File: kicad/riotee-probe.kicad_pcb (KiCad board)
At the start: 2 copper layers, 43.2 x 22.9 mm, 72 parts, among them J1 12402012E212A, J2 Conn_02x05_Odd_Even, J3 Conn_01x05, J4 Conn_01x05, U1 RP2040, U2 W25Q16JVUXIQ, U3 74LVC2T45GT, U4 74LVC2T45GT, U5 74LVC2T45GT, U6 74LVC2T45GT, U7 TLV73325PDBV, U8 TLV73333PDBV, Y1 Crystal_GND24

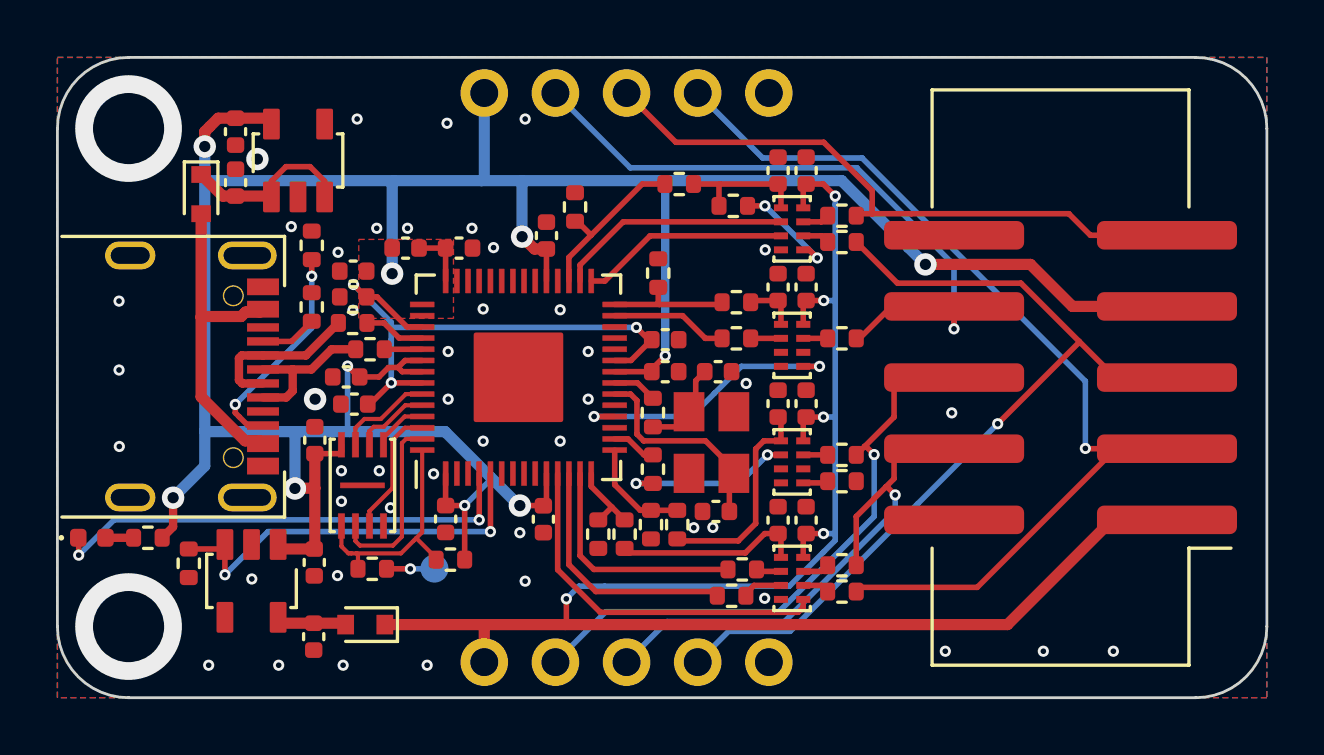
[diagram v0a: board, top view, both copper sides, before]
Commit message: add fourth level converter for simultaneous programming + TX/RX
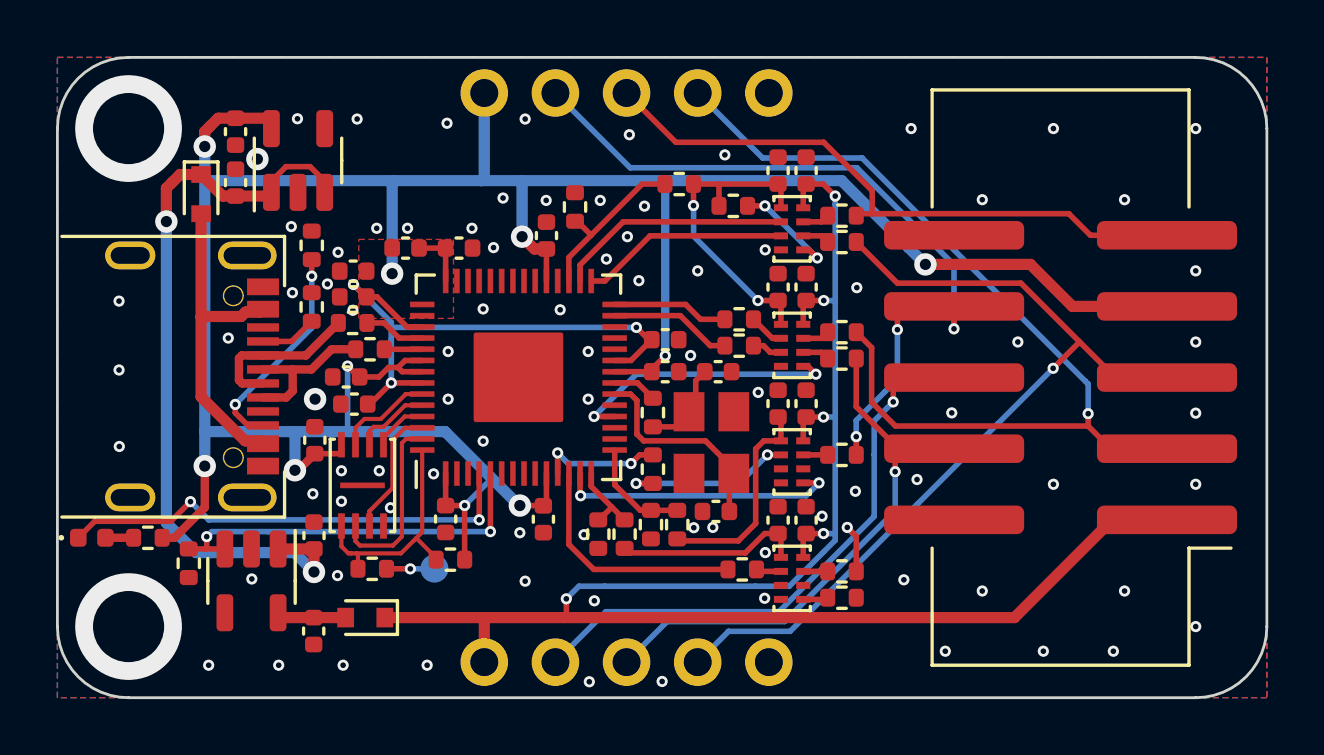
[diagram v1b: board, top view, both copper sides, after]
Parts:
- removed the R10 at (198.1, 67.8)
- removed the R18 at (199.2, 58.5)
- removed the R20 at (202.0, 59.5)
- removed the R8 at (197.1, 67.8)
- added R17: 5.1k, Resistor_SMD:R_0402_1005Metric, F.Cu at (197.1, 67.8)
- added R19: 120R, Resistor_SMD:R_0402_1005Metric, F.Cu at (198.1, 67.8)
- U7, U8: footprint riotee:TI_DBV0005A -> Package_TO_SOT_SMD:SOT-23-5
- moved R11 8.93 mm to (202.1, 61.1)
- moved R14 8.32 mm to (205.8, 60.6)
- moved R15 8.32 mm to (205.8, 61.5)
- moved R24 8.32 mm to (205.8, 69.2)
- moved R22 4.16 mm to (205.8, 70.1)
- moved C23 0.96 mm to (187.0, 67.9), turned to 90 degrees
- moved R10 0.69 mm to (202.1, 60.1)
- moved D3 0.25 mm to (188.8, 70.8)
- moved C25 0.20 mm to (186.9, 71.3)
- renumbered C19 to C16, C21 to C18, C20 to C19, C16 to C20, C22 to C21, C18 to C22, J4 to J2, J2 to J3, J3 to J4, R22 to R10, R13 to R11, R14 to R12, R15 to R13, R16 to R14, R17 to R15, R19 to R16, R21 to R18, R23 to R20, R12 to R21, R24 to R22, R26 to R23, R25 to R24, R27 to R25, R28 to R26, R29 to R27, R9 to R8, R11 to R9, U5 to U4, U6 to U5, U4 to U6
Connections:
- C16 pad 2: /LevelShifter/TransEnableDec3 -> /LevelShifter/TransEnableDec0
- C19 pad 2: /LevelShifter/TransEnableDec2 -> /LevelShifter/TransEnableDec1
- C20 pad 2: /LevelShifter/TransEnableDec1 -> /LevelShifter/TransEnableDec2
- C23 pad 1: +3V3 -> VBUS
- C24 pad 1: Net-(C24-Pad1) -> VBUS
- D2 pad 1: Net-(C24-Pad1) -> VBUS
- D2 pad 2: VBUS -> Net-(D2-Pad2)
- J1 pad A4/B9: VBUS -> Net-(D2-Pad2)
- J1 pad B4/A9: VBUS -> Net-(D2-Pad2)
- R10 pad 1: /Controller/UartTx -> /Controller/SbwOut.IO
- R11 pad 1: /Controller/SbwOut.IO -> /Controller/SwdOut.IO
- R11 pad 2: Net-(R13-Pad2) -> Net-(R11-Pad2)
- R14 pad 1: Net-(R16-Pad1) -> Net-(R14-Pad1)
- R14 pad 2: /Connectors/Target_SWD.IO -> /Connectors/Target_SBW.IO
- R15 pad 1: Net-(R17-Pad1) -> Net-(R15-Pad1)
- R15 pad 2: /Connectors/Target_SBW.IO -> /Connectors/Target_SWD.IO
- R16 pad 1: /Controller/TransEnable2 -> /Controller/TransEnable1
- R18 pad 1: /Controller/TransEnable2 -> /Controller/TransEnable1
- R18 pad 2: /LevelShifter/TransEnableDec2 -> /LevelShifter/TransEnableDec1
- R20 pad 1: /Controller/UartRx -> /Controller/UartTx
- R21 pad 1: /Controller/SwdOut.IO -> /Controller/UartRx
- R22 pad 2: Net-(R24-Pad2) -> Net-(R22-Pad2)
- R23 pad 2: /Connectors/Target_UART_TX -> /Connectors/Target_UART_RX
- R24 pad 1: Net-(R25-Pad1) -> Net-(R24-Pad1)
- R24 pad 2: /Connectors/Target_UART_RX -> /Connectors/Target_UART_TX
- U1 pad 11: /Controller/ProgDir -> /Controller/UartTx
- U1 pad 12: /Controller/SbwOut.IO -> /Controller/UartRx
- U1 pad 13: /Controller/SwdOut.IO -> /Controller/Trans_UARTRX_Dir
- U1 pad 14: /Controller/TransEnable1 -> /Controller/TransEnable2
- U1 pad 15: /Controller/TransEnable2 -> /Controller/TransEnable1
- U1 pad 16: /Controller/UartRx -> unconnected-(U1-Pad16)
- U1 pad 18: /Controller/Trans_UARTRX_Dir -> /Controller/ProgDir
- U1 pad 27: /Controller/UartTx -> /Controller/SwdOut.IO
- U1 pad 28: /Controller/TransEnable3 -> /Controller/SbwOut.IO
- U4 pad 1: /LevelShifter/TransEnableDec3 -> /LevelShifter/TransEnableDec0
- U4 pad 3: unconnected-(U5-Pad3) (its old number) -> Net-(R11-Pad2)
- U4 pad 5: /Controller/Trans_UARTRX_Dir -> /Controller/ProgDir
- U4 pad 6: unconnected-(U5-Pad6) (its old number) -> Net-(R15-Pad1)
- U4 pad 7: Net-(R25-Pad1) -> Net-(R14-Pad1)
- U5 pad 1: /LevelShifter/TransEnableDec2 -> /LevelShifter/TransEnableDec1
- U5 pad 5: Net-(R24-Pad2) -> /Controller/Trans_UARTRX_Dir
- U6 pad 1: /LevelShifter/TransEnableDec1 -> /LevelShifter/TransEnableDec2
- U6 pad 3: Net-(R13-Pad2) -> unconnected-(U6-Pad3)
- U6 pad 5: /Controller/ProgDir -> Net-(R22-Pad2)
- U6 pad 6: Net-(R17-Pad1) -> unconnected-(U6-Pad6)
- U6 pad 7: Net-(R16-Pad1) -> Net-(R24-Pad1)
- U7 pad 1: +3V3 -> VBUS
- U8 pad 1: Net-(C24-Pad1) -> VBUS
- U8 pad 3: Net-(C24-Pad1) -> VBUS
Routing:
- net VBUS: track 12.3 -> 27.5 mm, vias 0 -> 2
- net Net-(D2-Pad2): track 0.00 -> 12.3 mm
- net /Controller/UartRx: track 1.60 -> 8.58 mm
- net /LevelShifter/TransEnableDec0: track 4.70 -> 11.4 mm, vias 0 -> 2
- net Net-(C24-Pad1): track 6.01 -> 0.00 mm
- net +3V3: track 110.3 -> 105.1 mm
- net /Controller/SbwOut.IO: track 9.02 -> 4.15 mm
- net /Controller/TransEnable3: track 4.49 -> 0.00 mm
- net /Controller/SwdOut.IO: track 8.42 -> 4.38 mm
- net /Connectors/Target_UART_RX: track 23.8 -> 27.7 mm, vias 1 -> 3
- net /Controller/ProgDir: track 13.2 -> 9.85 mm, vias 0 -> 2
- net /Connectors/Target_SBW.IO: track 36.6 -> 33.7 mm
- net /Connectors/Target_SWD.IO: track 19.6 -> 21.8 mm
- net /LevelShifter/TransEnableDec3: track 1.90 -> 0.00 mm
- net /Connectors/Target_UART_TX: track 21.6 -> 22.9 mm, vias 1 -> 2
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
